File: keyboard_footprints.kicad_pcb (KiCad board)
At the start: 2 copper layers, 74.5 x 85 mm, 11 parts

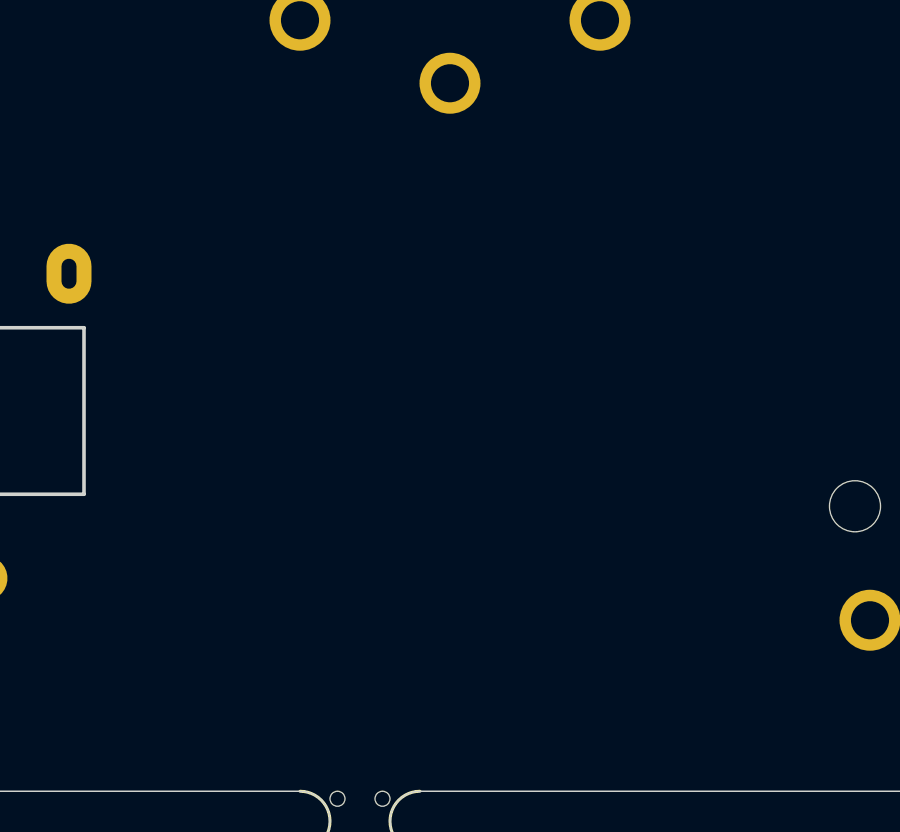
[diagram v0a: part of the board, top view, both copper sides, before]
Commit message: Create footprint for QFP/QFN MCU with all pins broken out
Supports
* STM32F072CBT6
* STM32F072CBU6
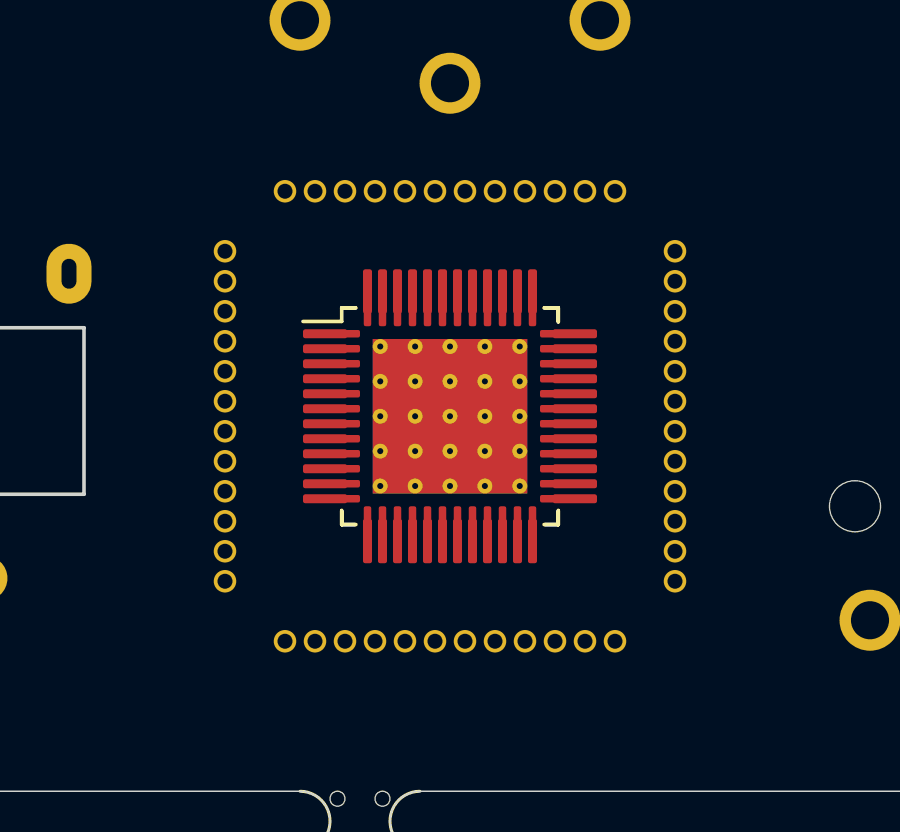
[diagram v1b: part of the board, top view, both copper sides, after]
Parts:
- added REF**: Dual_MCU_QFP_QFN_48_with_breakout_pins, breakout_pins:Dual_MCU_QFP_QFN_48_with_breakout_pins, F.Cu at (39.0, 38.0)
